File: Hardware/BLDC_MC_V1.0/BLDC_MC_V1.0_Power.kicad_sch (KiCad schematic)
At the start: 52 parts, among them Q7 BSC027N10NS5ATMA1, U1 LM76005RNPR, U16 LM74700QDRQ1, U5 LDL1117S33R, U7 NCV4274ADT50RKG

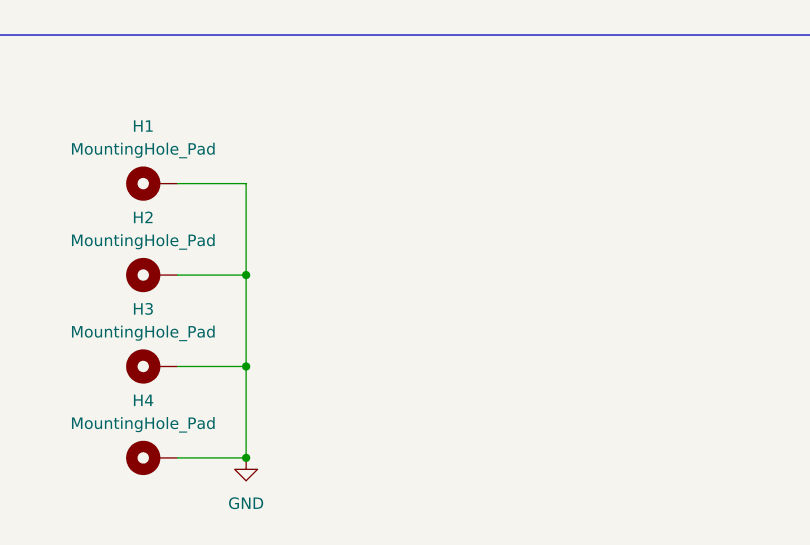
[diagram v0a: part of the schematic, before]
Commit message: Updated the design by adding chassis ground to the board
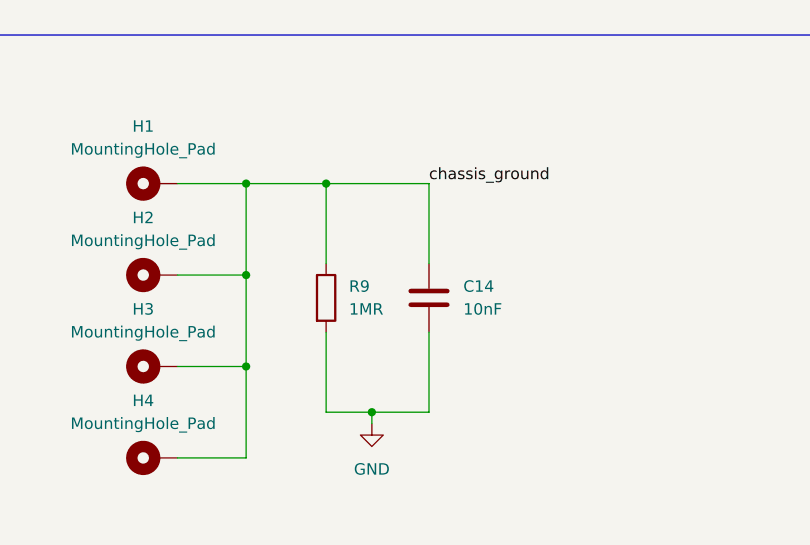
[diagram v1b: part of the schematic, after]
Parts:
- added C14: 10nF, Capacitor_SMD:C_1206_3216Metric, symbol Device:C
- added R9: 1MR, Resistor_SMD:R_1206_3216Metric, symbol Device:R
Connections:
- net GND: now also C14.2, R9.2; no longer H1.1, H2.1, H3.1, H4.1
- new net chassis_ground: C14.1, H1.1, H2.1, H3.1, H4.1, R9.1

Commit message: Updated the information box of the sheets
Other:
- note added: "[2] Power Conversion Vin to 12V and 5V to 3.3V"
- note removed: "[1] Power Conversion Vin to 12V and 5V to 3.3V"
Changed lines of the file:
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@@
 		(rev "V1.0")
 		(company "Ahmed Aboeita")
-		(comment 1 "8-Layer High-TG180 PCB with Kelvin Current Sensing")
-		(comment 2 "Power Stage: 3-Phase Inverter with Active Reverse Polarity & E-Fuse OCP")
-		(comment 3 "Core MCU: STM32G431RBT6 (FOC & CORDIC Processing, 100 kHz PWM)")
+		(comment 1 "8-Layer High-TG180 PCB with controlled impedance profile")
+		(comment 2 "Power Stage: 3-Phase Inverter with Active Reverse Polarity ")
+		(comment 3 "Core MCU: STM32G431RBT6 (FOC Processing, 100 kHz PWM)")
 		(comment 4 "Stackup & Sensing: System Ratings: 60V DC Bus | 30A Continuous | T_A = 125 degrees  ")
 	)
@@
 		)
 	)
-	(text "[1] Power Conversion Vin to 12V and 5V to 3.3V"
+	(text "[2] Power Conversion Vin to 12V and 5V to 3.3V"
 		(exclude_from_sim no)
 		(at 143.51 19.05 0)
